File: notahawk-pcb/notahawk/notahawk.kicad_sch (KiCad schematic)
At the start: 50 parts, among them J1 Conn_01x02_Pin, J2 USB-to-TTL cable, SW1 Reset button, SW2 Reset button, SW3 SW_SPST, U2 BNO085, U3 BMP581, U4 ADXL372BCCZ-RL7, U5 W25Q128JVSIQ, U6 ESP32-C3, Y1 ECS-TXO-2520-33-400-AN-TR

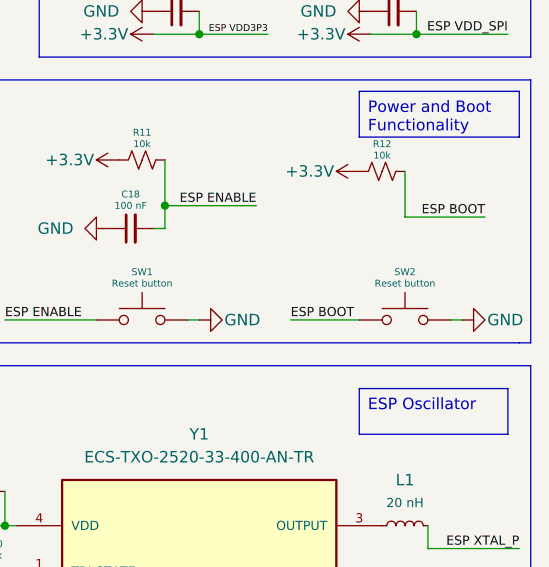
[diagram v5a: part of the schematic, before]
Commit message: footprints assigned, finished schematic for good, starting pcb
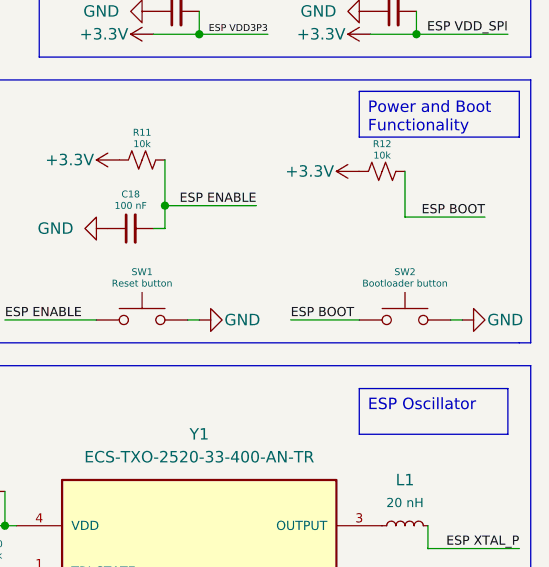
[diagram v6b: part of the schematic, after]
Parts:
- C1, C10, C11, C12, C13, C14, C15, C17, C18, C2, C3, C4, C5, C6, C7, C9: footprint (none) -> Capacitor_SMD:C_0402_1005Metric
- C16, C8: footprint (none) -> Capacitor_SMD:C_0603_1608Metric
- D2, D3, D4: footprint (none) -> LED_SMD:LED_0805_2012Metric
- PS1: footprint TSR_1-2433SM:CONV_TSR_1-2433SM -> regulators:CONV_TSR_1-2433SM
- R1, R10, R11, R12, R13, R14, R15, R2, R3, R4, R6, R7, R8, R9: footprint (none) -> Resistor_SMD:R_0603_1608Metric
- SW1: footprint (none) -> switches_additional:SW_TS02-66-50-BK-100-LCR-D
- SW2: value Reset button -> Bootloader button; footprint (none) -> switches_additional:SW_TS02-66-50-BK-100-LCR-D
- U2: footprint BNO085:IC_BNO085 -> sensor_motion_additional:IC_BNO085
- U3: footprint BMP581:BMP581 -> sensor_pressure_additional:BMP581
- U4: footprint ADXL372BCCZ-RL7:PQFN50P322X300X114-16N -> sensor_motion_additional:PQFN50P322X300X114-16N
- U5: footprint W25Q128JVSIQ:SOIC127P790X216-8N -> flash_memory_additional:SOIC127P790X216-8N
- U6: footprint ESP32-C3:QFN50P500X500X90-33N -> microcontrollers_additional:QFN50P500X500X90-33N
- Y1: footprint ECS-TXO-2520-33-400-AN-TR:OSC_ECS-TXO-2520-33-400-AN-TR -> crystals_additional:OSC_ECS-TXO-2520-33-400-AN-TR
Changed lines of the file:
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@@
 			)
 		)
-		(property "Footprint" ""
+		(property "Footprint" "Resistor_SMD:R_0603_1608Metric"
 			(at 135.89 105.41 0)
 			(effects
@@
 			)
 		)
-		(property "Footprint" ""
+		(property "Footprint" "Resistor_SMD:R_0603_1608Metric"
 			(at 31.75 166.37 0)
 			(effects
@@
 			)
 		)
-		(property "Footprint" ""
+		(property "Footprint" "Capacitor_SMD:C_0402_1005Metric"
 			(at 96.52 90.17 0)
 			(effects
@@
 			)
 		)
-		(property "Footprint" ""
+		(property "Footprint" "LED_SMD:LED_0805_2012Metric"
 			(at 148.59 157.48 0)
 			(effects
@@
 			)
 		)
-		(property "Footprint" ""
+		(property "Footprint" "Resistor_SMD:R_0603_1608Metric"
 			(at 240.03 107.95 0)
 			(effects
@@
 			)
 		)
-		(property "Value" "Reset button"
+		(property "Value" "Bootloader button"
 			(at 269.24 121.666 0)
 			(effects
@@
 			)
 		)
-		(property "Footprint" ""
+		(property "Footprint" "switches_additional:SW_TS02-66-50-BK-100-LCR-D"
 			(at 269.24 120.65 0)
 			(effects
@@
 			)
 		)
-		(property "Footprint" ""
+		(property "Footprint" "Capacitor_SMD:C_0402_1005Metric"
 			(at 43.18 33.02 0)
 			(effects
@@
 			)
 		)
-		(property "Footprint" "ECS-TXO-2520-33-400-AN-TR:OSC_ECS-TXO-2520-33-400-AN-TR"
+		(property "Footprint" "crystals_additional:OSC_ECS-TXO-2520-33-400-AN-TR"
 			(at 246.38 151.13 0)
 			(effects
@@
 			)
 		)
-		(property "Footprint" ""
+		(property "Footprint" "Capacitor_SMD:C_0402_1005Metric"
 			(at 33.02 44.45 0)
 			(effects
@@
 			)
 		)
-		(property "Footprint" ""
+		(property "Footprint" "Capacitor_SMD:C_0402_1005Metric"
 			(at 222.25 144.78 0)
 			(effects
@@
 			)
 		)
-		(property "Footprint" "BNO085:IC_BNO085"
+		(property "Footprint" "sensor_motion_additional:IC_BNO085"
 			(at 63.5 82.55 0)
 			(effects
@@
 			)
 		)
-		(property "Footprint" ""
+		(property "Footprint" "Resistor_SMD:R_0603_1608Metric"
 			(at 29.21 82.55 0)
 			(effects
@@
 			)
 		)
-		(property "Footprint" ""
+		(property "Footprint" "Capacitor_SMD:C_0402_1005Metric"
 			(at 238.76 115.57 0)
 			(effects
@@
 			)
 		)
-		(property "Footprint" "ESP32-C3:QFN50P500X500X90-33N"
+		(property "Footprint" "microcontrollers_additional:QFN50P500X500X90-33N"
 			(at 71.12 158.75 0)
 			(effects
@@
 			)
 		)
-		(property "Footprint" "BMP581:BMP581"
+		(property "Footprint" "sensor_pressure_additional:BMP581"
 			(at 62.23 36.83 0)
 			(effects
@@
 			)
 		)
-		(property "Footprint" ""
+		(property "Footprint" "Capacitor_SMD:C_0603_1608Metric"
 			(at 181.61 26.67 0)
 			(effects
@@
 			)
 		)
-		(property "Footprint" ""
+		(property "Footprint" "Capacitor_SMD:C_0402_1005Metric"
 			(at 265.43 73.66 0)
 			(effects
@@
 			)
 		)
-		(property "Footprint" ""
+		(property "Footprint" "Capacitor_SMD:C_0402_1005Metric"
 			(at 191.77 27.94 0)
 			(effects
@@
 			)
 		)
-		(property "Footprint" ""
+		(property "Footprint" "Capacitor_SMD:C_0402_1005Metric"
 			(at 243.84 82.55 0)
 			(effects
@@
 			)
 		)
-		(property "Footprint" "ADXL372BCCZ-RL7:PQFN50P322X300X114-16N"
+		(property "Footprint" "sensor_motion_additional:PQFN50P322X300X114-16N"
 			(at 158.75 44.45 0)
 			(effects
@@
 			)
 		)
-		(property "Footprint" ""
+		(property "Footprint" "Capacitor_SMD:C_0402_1005Metric"
 			(at 104.14 58.42 0)
 			(effects
@@
 			)
 		)
-		(property "Footprint" ""
+		(property "Footprint" "LED_SMD:LED_0805_2012Metric"
 			(at 186.69 157.48 0)
 			(effects
@@
 			)
 		)
-		(property "Footprint" ""
+		(property "Footprint" "Resistor_SMD:R_0603_1608Metric"
 			(at 35.56 149.86 0)
 			(effects
@@
 			)
 		)
-		(property "Footprint" ""
+		(property "Footprint" "Resistor_SMD:R_0603_1608Metric"
 			(at 35.56 158.75 0)
 			(effects
@@
 			)
 		)
-		(property "Footprint" "W25Q128JVSIQ:SOIC127P790X216-8N"
+		(property "Footprint" "flash_memory_additional:SOIC127P790X216-8N"
 			(at 170.18 95.25 0)
 			(effects
@@
 			)
 		)
-		(property "Footprint" ""
+		(property "Footprint" "Capacitor_SMD:C_0402_1005Metric"
 			(at 265.43 82.55 0)
 			(effects
@@
 			)
 		)
-		(property "Footprint" ""
+		(property "Footprint" "Resistor_SMD:R_0603_1608Metric"
 			(at 104.14 151.13 0)
 			(effects
@@
 			)
 		)
-		(property "Footprint" ""
+		(property "Footprint" "switches_additional:SW_TS02-66-50-BK-100-LCR-D"
 			(at 240.03 120.65 0)
 			(effects
@@
 			)
 		)
-		(property "Footprint" ""
+		(property "Footprint" "Resistor_SMD:R_0603_1608Metric"
 			(at 223.52 153.67 0)
 			(effects
@@
 			)
 		)
-		(property "Footprint" ""
+		(property "Footprint" "Resistor_SMD:R_0603_1608Metric"
 			(at 116.84 140.97 0)
 			(effects
@@
 			)
 		)
-		(property "Footprint" ""
+		(property "Footprint" "Capacitor_SMD:C_0402_1005Metric"
 			(at 243.84 91.44 0)
 			(effects
@@
 			)
 		)
-		(property "Footprint" ""
+		(property "Footprint" "Capacitor_SMD:C_0402_1005Metric"
 			(at 204.47 78.74 0)
 			(effects
@@
 			)
 		)
-		(property "Footprint" ""
+		(property "Footprint" "Resistor_SMD:R_0603_1608Metric"
 			(at 175.26 157.48 0)
 			(effects
@@
 			)
 		)
-		(property "Footprint" ""
+		(property "Footprint" "Resistor_SMD:R_0603_1608Metric"
 			(at 135.89 111.76 0)
 			(effects
@@
 			)
 		)
-		(property "Footprint" ""
+		(property "Footprint" "Resistor_SMD:R_0603_1608Metric"
 			(at 266.7 109.22 0)
 			(effects
@@
 			)
 		)
-		(property "Footprint" "TSR_1-2433SM:CONV_TSR_1-2433SM"
+		(property "Footprint" "regulators:CONV_TSR_1-2433SM"
 			(at 252.73 50.8 0)
 			(effects
@@
 			)
 		)
-		(property "Footprint" ""
+		(property "Footprint" "Capacitor_SMD:C_0402_1005Metric"
 			(at 104.14 72.39 0)
 			(effects
@@
 			)
 		)
-		(property "Footprint" ""
+		(property "Footprint" "Capacitor_SMD:C_0402_1005Metric"
 			(at 200.66 110.49 0)
 			(effects
@@
 			)
 		)
-		(property "Footprint" ""
+		(property "Footprint" "Resistor_SMD:R_0603_1608Metric"
 			(at 157.48 144.78 0)
 			(effects
@@
 			)
 		)
-		(property "Footprint" ""
+		(property "Footprint" "LED_SMD:LED_0805_2012Metric"
 			(at 166.37 144.78 0)
 			(effects
@@
 			)
 		)
-		(property "Footprint" ""
+		(property "Footprint" "Capacitor_SMD:C_0603_1608Metric"
 			(at 245.11 73.66 0)
 			(effects
@@
 			)
 		)
-		(property "Footprint" ""
+		(property "Footprint" "Capacitor_SMD:C_0402_1005Metric"
 			(at 184.15 41.91 0)
 			(effects
@@
 			)
 		)
-		(property "Footprint" ""
+		(property "Footprint" "Capacitor_SMD:C_0402_1005Metric"
 			(at 267.97 91.44 0)
 			(effects
@@
 			)
 		)
-		(property "Footprint" ""
+		(property "Footprint" "Resistor_SMD:R_0603_1608Metric"
 			(at 29.21 91.44 0)
 			(effects
